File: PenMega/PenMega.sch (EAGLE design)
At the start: 18 parts, among them IC2 REG1117, U1 ATMEGA328P_TQFP, U2 USD-SOCKET, Y1 16MHZ

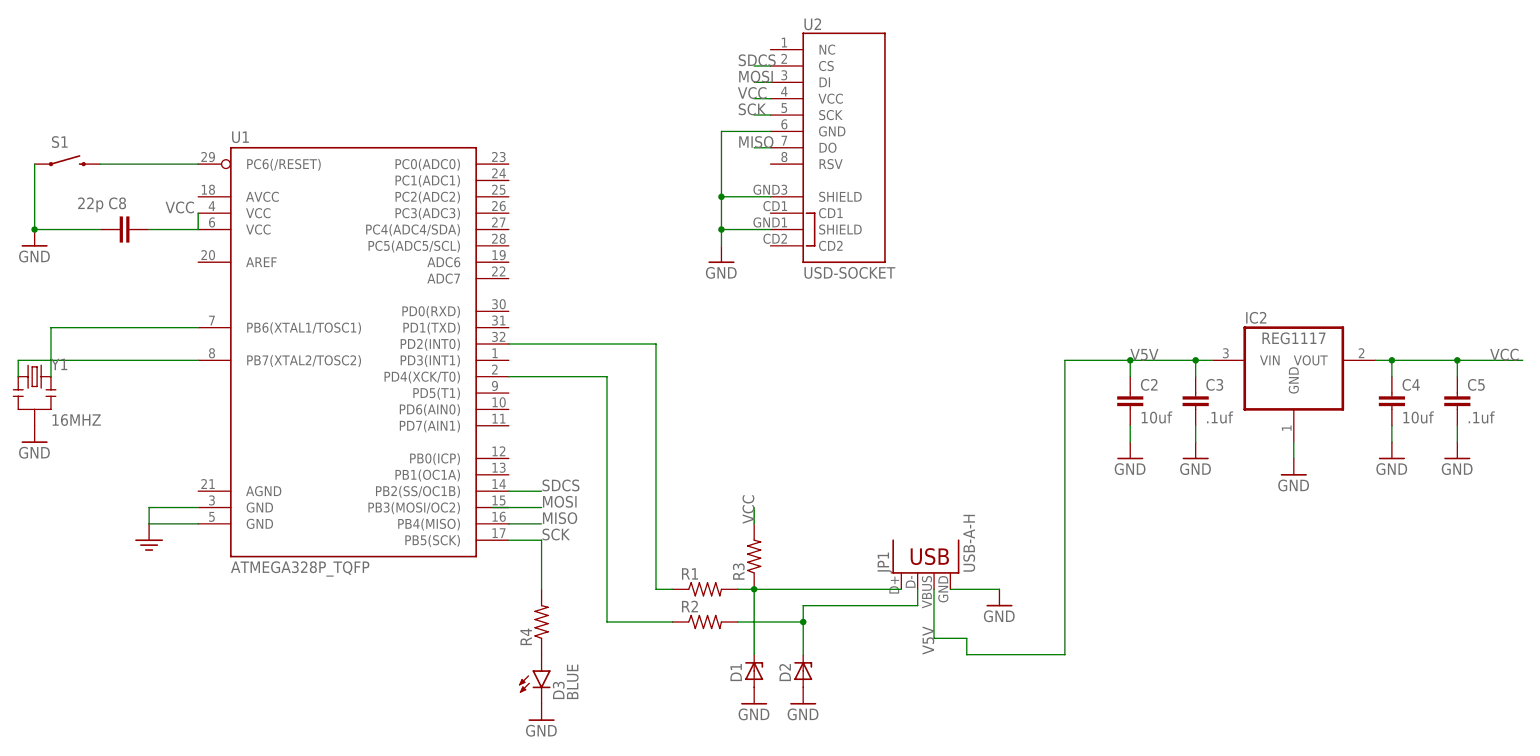
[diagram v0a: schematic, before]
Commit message: Trying to make this work, as of now first sent to manufacturing did not work with 6mills paths. changed to 10 mills.
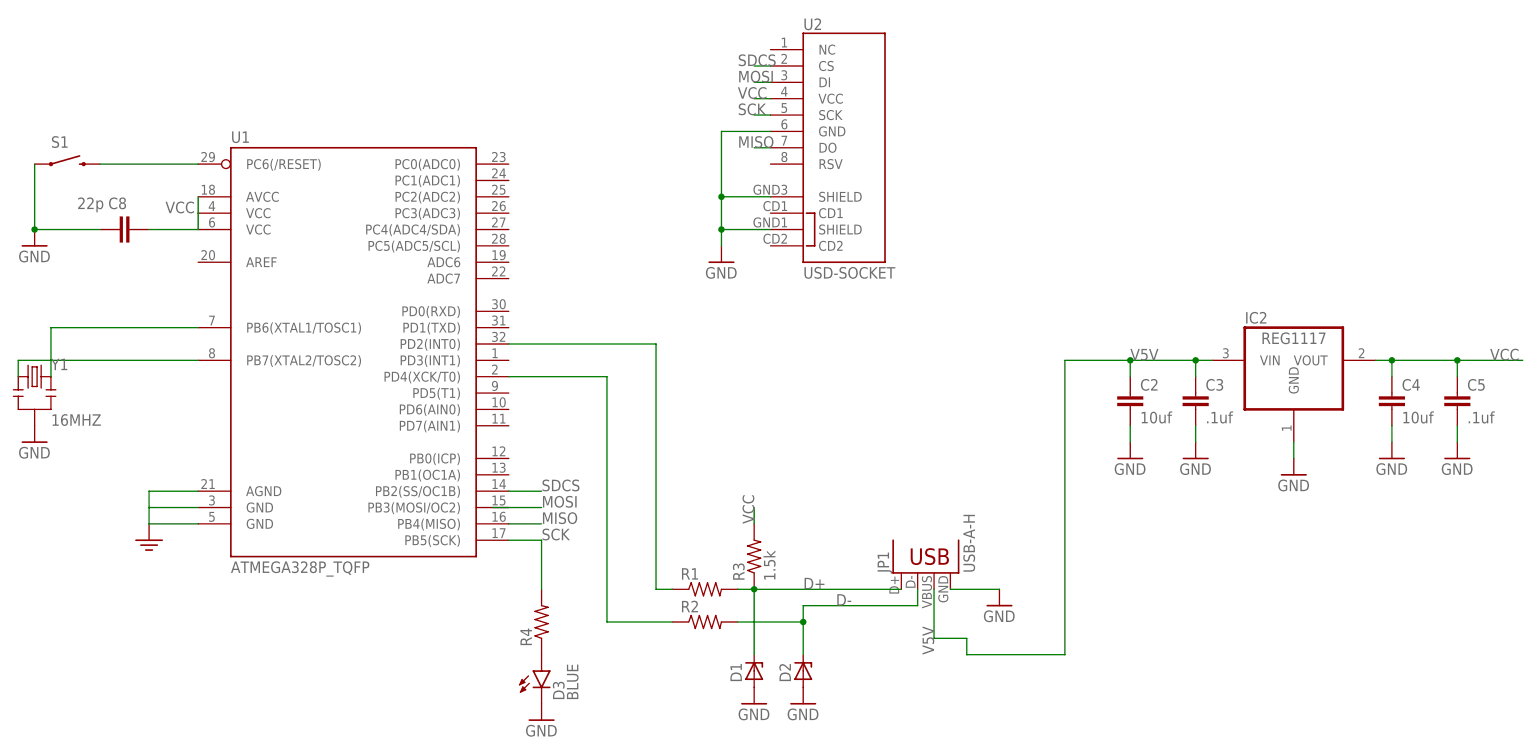
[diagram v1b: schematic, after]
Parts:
- R3: value (none) -> 1.5k
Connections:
- net N$3 renamed D+
- net N$4 renamed D-
- net GND: now also U1.AGND
- net VCC: now also U1.AVCC
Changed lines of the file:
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@@
 <part name="R1" library="SparkFun-Passives" deviceset="RESISTOR" device="0603-RES"/>
 <part name="R2" library="SparkFun-Passives" deviceset="RESISTOR" device="0603-RES"/>
-<part name="R3" library="SparkFun-Passives" deviceset="RESISTOR" device="0603-RES"/>
+<part name="R3" library="SparkFun-Passives" deviceset="RESISTOR" device="0603-RES" value="1.5k"/>
 <part name="R4" library="SparkFun-Passives" deviceset="RESISTOR" device="0603-RES"/>
 <part name="D1" library="digital-ic" deviceset="ZENER-DIODE" device="SMB"/>
@@
 </busses>
 <nets>
-<net name="N$3" class="0">
+<net name="D+" class="0">
 <segment>
 <pinref part="JP1" gate="G$1" pin="D+"/>
@@
 <junction x="106.68" y="7.62"/>
 <pinref part="R3" gate="G$1" pin="1"/>
-</segment>
-</net>
-<net name="N$4" class="0">
+<label x="114.3" y="7.62" size="1.778" layer="95"/>
+</segment>
+</net>
+<net name="D-" class="0">
 <segment>
 <pinref part="R2" gate="G$1" pin="2"/>
@@
 <wire x1="114.3" y1="-2.54" x2="114.3" y2="2.54" width="0.1524" layer="91"/>
 <junction x="114.3" y="2.54"/>
+<label x="119.38" y="5.08" size="1.778" layer="95"/>
 </segment>
 </net>
@@
 <wire x1="20.32" y1="20.32" x2="12.7" y2="20.32" width="0.1524" layer="91"/>
 <wire x1="12.7" y1="20.32" x2="12.7" y2="17.78" width="0.1524" layer="91"/>
+<pinref part="U1" gate="U$1" pin="AGND"/>
+<wire x1="20.32" y1="22.86" x2="12.7" y2="22.86" width="0.1524" layer="91"/>
+<wire x1="12.7" y1="22.86" x2="12.7" y2="20.32" width="0.1524" layer="91"/>
 </segment>
 <segment>
@@
 <pinref part="C8" gate="G$1" pin="1"/>
 <wire x1="20.32" y1="63.5" x2="12.7" y2="63.5" width="0.1524" layer="91"/>
-</segment>
-<segment>
+<pinref part="U1" gate="U$1" pin="AVCC"/>
+<wire x1="20.32" y1="68.58" x2="20.32" y2="66.04" width="0.1524" layer="91"/>
+</segment>
+<segment>

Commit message: Partial fix for penmega. Removed un needed zener diodes
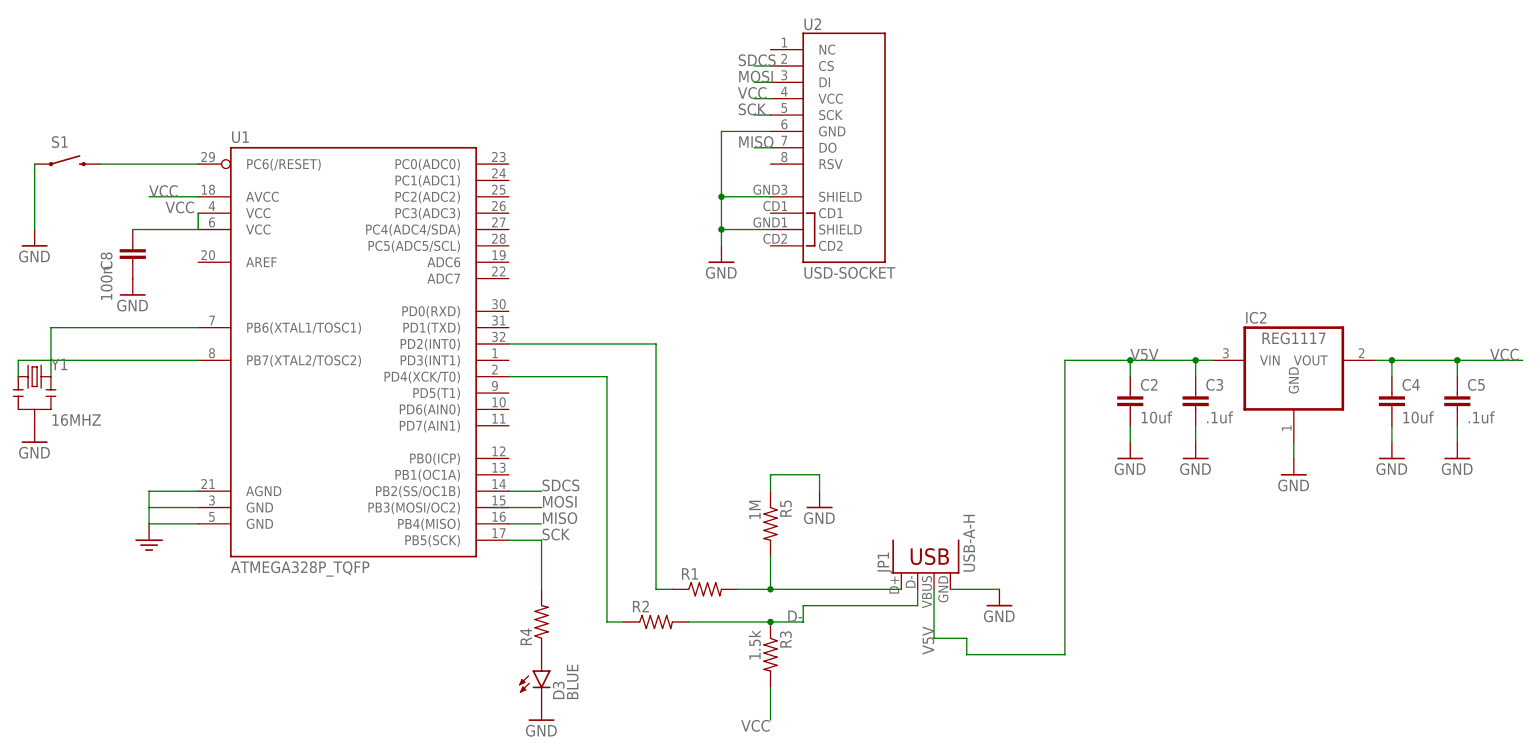
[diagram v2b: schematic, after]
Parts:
- removed D1, D2: (no value), digital-ic:ZENER-DIODESMB
- added R5: 1M, SparkFun-Passives:RESISTOR0603-RES
- C8: value 22p -> 100n
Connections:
- removed net D+: D1.C, JP1.D+, R1.2, R3.1
- new net N$3: JP1.D+, R1.2, R5.2
- net D-: now also R3.1; no longer D2.C
- net GND: now also R5.1; no longer D1.A, D2.A
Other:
- moved on the sheet: C8, R2, R3
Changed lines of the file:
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@@
 <part name="R3" library="SparkFun-Passives" deviceset="RESISTOR" device="0603-RES" value="1.5k"/>
 <part name="R4" library="SparkFun-Passives" deviceset="RESISTOR" device="0603-RES"/>
-<part name="D1" library="digital-ic" deviceset="ZENER-DIODE" device="SMB"/>
-<part name="D2" library="digital-ic" deviceset="ZENER-DIODE" device="SMB"/>
 <part name="S1" library="SparkFun-Electromechanical" deviceset="SWITCH-MOMENTARY-2" device="SMD" value="SWITCH-MOMENTARY-2SMD"/>
 <part name="GND1" library="SparkFun-Aesthetics" deviceset="GND" device=""/>
 <part name="GND6" library="SparkFun-Aesthetics" deviceset="GND" device=""/>
-<part name="GND3" library="SparkFun-Aesthetics" deviceset="GND" device=""/>
-<part name="GND4" library="SparkFun-Aesthetics" deviceset="GND" device=""/>
 <part name="GND5" library="SparkFun-Aesthetics" deviceset="GND" device=""/>
 <part name="D3" library="SparkFun-LED" deviceset="LED-BLUE" device="0603" value="BLUE"/>
@@
 <part name="GND10" library="supply1" deviceset="GND" device=""/>
 <part name="GND11" library="SparkFun-Aesthetics" deviceset="GND" device=""/>
-<part name="C8" library="SparkFun-Passives" deviceset="CAP" device="0603-CAP" value="22p"/>
+<part name="C8" library="SparkFun-Passives" deviceset="CAP" device="0603-CAP" value="100n"/>
+<part name="GND12" library="SparkFun-Aesthetics" deviceset="GND" device=""/>
+<part name="R5" library="SparkFun-Passives" deviceset="RESISTOR" device="0603-RES" value="1M"/>
+<part name="GND13" library="SparkFun-Aesthetics" deviceset="GND" device=""/>
 </parts>
 <sheets>
@@
 <instance part="JP1" gate="G$1" x="137.16" y="10.16" rot="R90"/>
 <instance part="R1" gate="G$1" x="99.06" y="7.62"/>
-<instance part="R2" gate="G$1" x="99.06" y="2.54"/>
-<instance part="R3" gate="G$1" x="106.68" y="12.7" rot="R90"/>
+<instance part="R2" gate="G$1" x="91.44" y="2.54"/>
+<instance part="R3" gate="G$1" x="109.22" y="-2.54" rot="R270"/>
 <instance part="R4" gate="G$1" x="73.66" y="2.54" rot="R90"/>
-<instance part="D1" gate="G$1" x="106.68" y="-5.08" rot="R90"/>
-<instance part="D2" gate="G$1" x="114.3" y="-5.08" rot="R90"/>
 <instance part="S1" gate="G$1" x="0" y="73.66" smashed="yes">
 <attribute name="NAME" x="-2.54" y="76.2" size="1.778" layer="95"/>
@@
 <instance part="GND1" gate="1" x="-5.08" y="60.96"/>
 <instance part="GND6" gate="1" x="-5.08" y="30.48"/>
-<instance part="GND3" gate="1" x="106.68" y="-10.16"/>
-<instance part="GND4" gate="1" x="114.3" y="-10.16"/>
 <instance part="GND5" gate="1" x="144.78" y="5.08"/>
 <instance part="D3" gate="G$1" x="73.66" y="-5.08"/>
@@
 <instance part="GND10" gate="1" x="215.9" y="27.94"/>
 <instance part="GND11" gate="1" x="101.6" y="58.42"/>
-<instance part="C8" gate="G$1" x="7.62" y="63.5" smashed="yes" rot="R270">
-<attribute name="NAME" x="6.35" y="66.675" size="1.778" layer="95"/>
-<attribute name="VALUE" x="1.524" y="66.675" size="1.778" layer="96"/>
+<instance part="C8" gate="G$1" x="10.16" y="58.42" smashed="yes">
+<attribute name="NAME" x="6.985" y="57.15" size="1.778" layer="95" rot="R90"/>
+<attribute name="VALUE" x="6.985" y="52.324" size="1.778" layer="96" rot="R90"/>
 </instance>
+<instance part="GND12" gate="1" x="10.16" y="53.34"/>
+<instance part="R5" gate="G$1" x="109.22" y="17.78" rot="R270"/>
+<instance part="GND13" gate="1" x="116.84" y="20.32"/>
 </instances>
 <busses>
 </busses>
 <nets>
-<net name="D+" class="0">
-<segment>
-<pinref part="JP1" gate="G$1" pin="D+"/>
-<pinref part="R1" gate="G$1" pin="2"/>
-<wire x1="129.54" y1="7.62" x2="106.68" y2="7.62" width="0.1524" layer="91"/>
-<pinref part="D1" gate="G$1" pin="C"/>
-<wire x1="106.68" y1="7.62" x2="104.14" y2="7.62" width="0.1524" layer="91"/>
-<wire x1="106.68" y1="-2.54" x2="106.68" y2="7.62" width="0.1524" layer="91"/>
-<junction x="106.68" y="7.62"/>
-<pinref part="R3" gate="G$1" pin="1"/>
-<label x="114.3" y="7.62" size="1.778" layer="95"/>
-</segment>
-</net>
 <net name="D-" class="0">
 <segment>
-<pinref part="R2" gate="G$1" pin="2"/>
-<wire x1="104.14" y1="2.54" x2="114.3" y2="2.54" width="0.1524" layer="91"/>
+<wire x1="109.22" y1="2.54" x2="114.3" y2="2.54" width="0.1524" layer="91"/>
 <wire x1="114.3" y1="2.54" x2="114.3" y2="5.08" width="0.1524" layer="91"/>
 <pinref part="JP1" gate="G$1" pin="D-"/>
 <wire x1="114.3" y1="5.08" x2="132.08" y2="5.08" width="0.1524" layer="91"/>
 <wire x1="132.08" y1="5.08" x2="132.08" y2="7.62" width="0.1524" layer="91"/>
-<pinref part="D2" gate="G$1" pin="C"/>
-<wire x1="114.3" y1="-2.54" x2="114.3" y2="2.54" width="0.1524" layer="91"/>
-<junction x="114.3" y="2.54"/>
-<label x="119.38" y="5.08" size="1.778" layer="95"/>
+<label x="111.76" y="2.54" size="1.778" layer="95"/>
+<pinref part="R3" gate="G$1" pin="1"/>
+<pinref part="R2" gate="G$1" pin="2"/>
+<wire x1="96.52" y1="2.54" x2="109.22" y2="2.54" width="0.1524" layer="91"/>
+<junction x="109.22" y="2.54"/>
 </segment>
 </net>
@@
 <wire x1="83.82" y1="40.64" x2="83.82" y2="2.54" width="0.1524" layer="91"/>
 <pinref part="R2" gate="G$1" pin="1"/>
-<wire x1="83.82" y1="2.54" x2="93.98" y2="2.54" width="0.1524" layer="91"/>
+<wire x1="83.82" y1="2.54" x2="86.36" y2="2.54" width="0.1524" layer="91"/>
 </segment>
 </net>
@@
 <wire x1="-5.08" y1="63.5" x2="-5.08" y2="73.66" width="0.1524" layer="91"/>
 <pinref part="GND1" gate="1" pin="GND"/>
-<pinref part="C8" gate="G$1" pin="2"/>
-<wire x1="5.08" y1="63.5" x2="-5.08" y2="63.5" width="0.1524" layer="91"/>
-<junction x="-5.08" y="63.5"/>
 </segment>
 <segment>
 <pinref part="Y1" gate="G$1" pin="2"/>
 <pinref part="GND6" gate="1" pin="GND"/>
-</segment>
-<segment>
-<pinref part="D1" gate="G$1" pin="A"/>
-<pinref part="GND3" gate="1" pin="GND"/>
-</segment>
-<segment>
-<pinref part="D2" gate="G$1" pin="A"/>
-<pinref part="GND4" gate="1" pin="GND"/>
 </segment>
 <segment>
@@
 <junction x="101.6" y="68.58"/>
 </segment>
+<segment>
+<pinref part="C8" gate="G$1" pin="2"/>
+<pinref part="GND12" gate="1" pin="GND"/>
+</segment>
+<segment>
+<pinref part="R5" gate="G$1" pin="1"/>
+<wire x1="109.22" y1="22.86" x2="109.22" y2="25.4" width="0.1524" layer="91"/>
+<pinref part="GND13" gate="1" pin="GND"/>
+<wire x1="109.22" y1="25.4" x2="116.84" y2="25.4" width="0.1524" layer="91"/>
+<wire x1="116.84" y1="25.4" x2="116.84" y2="22.86" width="0.1524" layer="91"/>
+</segment>
 </net>
 <net name="N$12" class="0">
@@
 <label x="15.24" y="66.04" size="1.778" layer="95"/>
 <pinref part="C8" gate="G$1" pin="1"/>
-<wire x1="20.32" y1="63.5" x2="12.7" y2="63.5" width="0.1524" layer="91"/>
-<pinref part="U1" gate="U$1" pin="AVCC"/>
-<wire x1="20.32" y1="68.58" x2="20.32" y2="66.04" width="0.1524" layer="91"/>
+<wire x1="20.32" y1="63.5" x2="10.16" y2="63.5" width="0.1524" layer="91"/>
 </segment>
 <segment>
@@
 <segment>
 <pinref part="R3" gate="G$1" pin="2"/>
-<wire x1="106.68" y1="17.78" x2="106.68" y2="20.32" width="0.1524" layer="91"/>
-<label x="106.68" y="17.78" size="1.778" layer="95" rot="R90"/>
+<wire x1="109.22" y1="-7.62" x2="109.22" y2="-12.7" width="0.1524" layer="91"/>
+<label x="109.22" y="-12.7" size="1.778" layer="95" rot="R180"/>
+</segment>
+<segment>
+<pinref part="U1" gate="U$1" pin="AVCC"/>
+<wire x1="20.32" y1="68.58" x2="12.7" y2="68.58" width="0.1524" layer="91"/>
+<label x="12.7" y="68.58" size="1.778" layer="95"/>
 </segment>
 </net>
@@
 </segment>
 </net>
+<net name="N$3" class="0">
+<segment>
+<pinref part="JP1" gate="G$1" pin="D+"/>
+<pinref part="R1" gate="G$1" pin="2"/>
+<wire x1="129.54" y1="7.62" x2="109.22" y2="7.62" width="0.1524" layer="91"/>
+<wire x1="109.22" y1="7.62" x2="104.14" y2="7.62" width="0.1524" layer="91"/>
+<pinref part="R5" gate="G$1" pin="2"/>
+<wire x1="109.22" y1="7.62" x2="109.22" y2="12.7" width="0.1524" layer="91"/>
+<junction x="109.22" y="7.62"/>
+</segment>
+</net>

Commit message: Partially working on fixing PenMega. Work in progress
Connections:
- net GND: now also U2.CD1, U2.CD2
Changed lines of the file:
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@@
 <pinref part="GND11" gate="1" pin="GND"/>
 <wire x1="109.22" y1="68.58" x2="101.6" y2="68.58" width="0.1524" layer="91"/>
-<wire x1="101.6" y1="68.58" x2="101.6" y2="63.5" width="0.1524" layer="91"/>
 <pinref part="U2" gate="G$1" pin="SHIELD@3"/>
+<wire x1="101.6" y1="66.04" x2="101.6" y2="63.5" width="0.1524" layer="91"/>
 <wire x1="109.22" y1="63.5" x2="101.6" y2="63.5" width="0.1524" layer="91"/>
 <wire x1="101.6" y1="63.5" x2="101.6" y2="60.96" width="0.1524" layer="91"/>
@@
 <wire x1="101.6" y1="78.74" x2="101.6" y2="68.58" width="0.1524" layer="91"/>
 <junction x="101.6" y="68.58"/>
+<wire x1="101.6" y1="66.04" x2="101.6" y2="68.58" width="0.1524" layer="91"/>
+<junction x="101.6" y="66.04"/>
+<pinref part="U2" gate="G$1" pin="CD1"/>
+<wire x1="109.22" y1="66.04" x2="101.6" y2="66.04" width="0.1524" layer="91"/>
+<pinref part="U2" gate="G$1" pin="CD2"/>
+<wire x1="109.22" y1="60.96" x2="101.6" y2="60.96" width="0.1524" layer="91"/>
+<junction x="101.6" y="60.96"/>
 </segment>
 <segment>
